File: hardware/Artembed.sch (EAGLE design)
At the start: 88 parts, among them J3 CORTEX_JTAG_DEBUG_MINIMUM_PTH, J4 CORTEX_JTAG_DEBUG_PTH_NS, J7 CAMERA-HIMAX, U1 DAPLINK_KL26Z, U2 16MHz, U3 ARTEMIS_MODULESMD, U4 1.8V, U5 LIS2DH12, Y1 32.768kHz

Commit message: Pre proto review
Waiting on XTAL footprint update from Eli
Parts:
- removed TP2: TEST-POINT3X5, SparkFun-Connectors:TEST-POINT3X5
- added R32, R33, R34: DNP, SparkFun-Resistors:RESISTOR0603
- C10, C9: value 8pF -> 12pF; device SparkFun-Capacitors:CAP-0603 -> SparkFun-Capacitors:12PF-0603-50V-5%
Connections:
- removed net D1_SLSDA: J5.1
- removed net D2_SLSCL: J5.2
- removed net D3_PWM_UARTTX: J5.3, U3.~AD35(TX1/I2SDAT/PDMCLK)
- removed net D4_MISO: J5.4, U3.(SDA0/MISO0/I2SDAT)~D6
- removed net D5_MOSI_CLKOUT: J5.5, U3.(MOSI0/CLKOUT)~D7
- removed net D6_SCLK: J5.6, U3.(SCL0/SCK0)~D5
- removed net SCL_INTERNAL: ECC1.SCL, J7.SCL, U3.(SCL2/SCK2)~D27, U5.SCL/SPC
- removed net SDA_INTERNAL: ECC1.SDA, J7.SDA, U3.(SDA2/MISO2/RX1)~D25, U5.SDA/SDI/SDO
- new net D1: J9.1, U3.~AD29(PDMDATA)
- new net D2: J5.2, U3.~AD13(I2SBCLK/RX1)
- new net D3: J9.2, U3.(SDA2/MISO2/RX1)~D25
- new net D4: J5.3, U3.(SDA0/MISO0/I2SDAT)~D6
- new net D5: J9.3, U3.(SCL2/SCK2)~D27
- new net D6: J5.4, U3.(RX1/SLINT)~D4
- net CAMERA_D0: now also U3.(SDA3/MISO3/RX1)~D43; no longer U3.(MOSI3/RX1)D38
- net CAMERA_D1: now also U3.AD34(CMPRF2/PDMDATA); no longer U3.(SCL4/SCK4/TX1)~D39
- net CAMERA_D2: now also U3.~AD31(SCCCLK); no longer U3.(SDA4/MISO4/RX1)D40
- net CAMERA_D3: now also U3.~AD33(SWO/32KHZ); no longer U3.(BLEIF_IRQ/SWO/I2SWCLK)D41
- net CAMERA_D4: now also U3.(BLEIF_IRQ/SWO/I2SWCLK)D41; no longer U3.(SCL3/SCK3/TX1)~D42
- net CAMERA_D5: now also U3.(MOSI4)~D44; no longer U3.(SDA3/MISO3/RX1)~D43
- net CAMERA_D6: now also U3.(TX1/PDMCLK/SCCIO)~D37; no longer U3.(MOSI4)~D44
- net CAMERA_DVDD_EN: no longer U3.(MOSI1/TX1/PDMCLK)D10
- net CAMERA_HSYNC: now also U3.(SCL3/SCK3/TX1)~D42; no longer U3.(RX1/TRIG1/PDMDATA)D36
- net CAMERA_INT: now also U3.(MOSI3/RX1)D38; no longer U3.(TX1/32KHZ/SWO)~D24
- net CAMERA_MCLK: now also U3.(CMPIN1/SCCIO)~D18; no longer U3.(SCCRST)~D26
- net CAMERA_PCLK: now also U3.(RX1/TRIG1/PDMDATA)D36; no longer U3.(MOSI2/I2SWCLK)~D28
- net CAMERA_TRIG: now also U3.(CMPRF1/TRIG1/SCCCLK)D17; no longer U3.(I2SWCLK/CMPOUT)~D23
- net CAMERA_VSYNC: now also U3.AD16(TRIG0/SCCRST); no longer U3.(TX1/PDMCLK/SCCIO)~D37
- net D10: now also J5.6, U3.(SLMISO)D2; no longer J9.4, U3.(SLNCE/I2SWCLK)D3
- net D11: now also J9.6, U3.(SLMOSI/SLSDA)D1; no longer J9.5, U3.(SLMISO)D2
- net D12: now also J5.7, U3.(SLSCK/SLSCL/CLKOUT)D0; no longer J9.6, U3.(SLMOSI/SLSDA)D1
- net D13: now also U3.(SLNCE/I2SWCLK)D3; no longer U3.(SLSCK/SLSCL/CLKOUT)D0
- net D7: now also J9.4, U3.~AD35(TX1/I2SDAT/PDMCLK); no longer J9.1, U3.~AD13(I2SBCLK/RX1)
- net D8: now also J5.5, U3.(MOSI0/CLKOUT)~D7; no longer J9.2, U3.~AD29(PDMDATA)
- net D9: now also J9.5, U3.(SCL0/SCK0)~D5; no longer J9.3, U3.(RX1/SLINT)~D4
- net N$20: no longer TP2.1
- net SCL: now also ECC1.SCL, J7.SCL, U5.SCL/SPC
- net SDA: now also ECC1.SDA, J7.SDA, U5.SDA/SDI/SDO
- net TGT_SWCLK: now also R33.1
- net TGT_SWDIO: now also R32.1
- net TGT_SWO: now also R34.1
- net VDD: now also J5.1, R32.2, R33.2, R34.2; no longer J5.7
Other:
- moved on the sheet: J3, J5, J9

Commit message: proto review revisions, panelized, cammed
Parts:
- added FD1, FD2, FD3, FD4: FIDUCIAL0.2MM, SparkFun-Aesthetics:FIDUCIAL0.2MM
- added LOGO1: OSHW-LOGOS, SparkFun-Aesthetics:OSHW-LOGOS
- added LOGO2: SFE_LOGO_NAME.2_INCH, SparkFun-Aesthetics:SFE_LOGO_NAME.2_INCH
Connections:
- net CAMERA_DVDD_EN: now also U3.(ADCD1N/RX1/PDMDATA)D15

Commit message: initial commit of v02 schematic
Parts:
- removed C21: 1.0uF, SparkFun-Capacitors:1.0UF-0603-16V-10%
- removed D7: RED, SparkFun-LED:LED-RED0603
- removed E2: SPH0641LM4H-1, SparkFun-Sensors:SPH0641LM4H-1_MICROPHONE
- removed ECC1: ATECC508AUDFN_2X3MM, ATECC508A:ATECC508AUDFN_2X3MM
- removed FD1, FD2, FD3, FD4: FIDUCIAL0.2MM, SparkFun-Aesthetics:FIDUCIAL0.2MM
- removed JP1: HW/SW RESET, SparkFun-Jumpers:JUMPER-SMT_3_1-NC_TRACE_SILK
- removed LOGO1: OSHW-LOGOS, SparkFun-Aesthetics:OSHW-LOGOS
- removed LOGO2: SFE_LOGO_NAME.2_INCH, SparkFun-Aesthetics:SFE_LOGO_NAME.2_INCH
- removed R21: 2.2k, SparkFun-Resistors:2.2KOHM-0603-1/10W-1%
- removed R22, R30: 10k, SparkFun-Resistors:10KOHM-0603-1/10W-1%
- removed R23, R29: 33, SparkFun-Resistors:33OHM-0603-1/10W-1%
- removed R24: 10, SparkFun-Resistors:10OHM-0603-1/10W-1%
- removed R25, R26, R27, R28: 330, SparkFun-Resistors:330OHM-0603-1/10W-1%
- removed R32, R33, R34: DNP, SparkFun-Resistors:RESISTOR0603
- removed S3: RESET IF, SparkFun-Switches:MOMENTARY-SWITCH-SPST-SMD-4.6X2.8MM
- removed TP12, TP13: TEST-POINT3X5, SparkFun-Connectors:TEST-POINT3X5
- removed U5: LIS2DH12, SparkFun-Sensors:LIS2DH12
- added E1: SPH0641LM4H-1, SparkFun-Sensors:SPH0641LM4H-1_MICROPHONE
- added J10: (no value), SparkFun-Connectors:CONN_08SMD-STRAIGHT-FEMALE
- added S1: DIP-04SMD, SparkFun-Switches:DIP-04SMD
- added X1: 16MHz, SparkFun-Clocks:CRYSTAL-16MHZ_SMALL
- C1, C17: value 0.1uF -> 10uF; device SparkFun-Capacitors:0.1UF-0603-25V-5% -> SparkFun-Capacitors:10UF-0603-6.3V-20%
- C10: value 12pF -> 15pF; device SparkFun-Capacitors:12PF-0603-50V-5% -> SparkFun-Capacitors:15PF-0603-50V-5%
- C11: value 0.1uF -> 15pF; device SparkFun-Capacitors:0.1UF-0603-25V-5% -> SparkFun-Capacitors:15PF-0603-50V-5%
- C14: value 15pF -> 0.1uF; device SparkFun-Capacitors:15PF-0603-50V-5% -> SparkFun-Capacitors:0.1UF-0603-25V-5%
- C15: value 15pF -> 1.0uF; device SparkFun-Capacitors:15PF-0603-50V-5% -> SparkFun-Capacitors:1.0UF-0603-16V-10%
- C16, C3: value 1.0uF -> 0.1uF; device SparkFun-Capacitors:1.0UF-0603-16V-10% -> SparkFun-Capacitors:0.1UF-0603-25V-5%
- C18, C2: value 10uF -> 1.0uF; device SparkFun-Capacitors:10UF-0603-6.3V-20% -> SparkFun-Capacitors:1.0UF-0603-16V-10%
- C5: value 1nF -> 2.2uF; device SparkFun-Capacitors:1.0NF/1000PF-0603-50V-10% -> SparkFun-Capacitors:2.2UF-0603-10V-20%
- C6: value 2.2uF -> 0.1uF; device SparkFun-Capacitors:2.2UF-0603-10V-20% -> SparkFun-Capacitors:0.1UF-0603-25V-5%
- C8: value 0.1uF -> 12pF; device SparkFun-Capacitors:0.1UF-0603-25V-5% -> SparkFun-Capacitors:12PF-0603-50V-5%
- D1: value 3A/10V/280mV -> BLUE; device SparkFun-DiscreteSemi:DIODE-SCHOTTKY-BAT60A -> SparkFun-LED:LED-BLUE0603
- D2: value 3A/10V/280mV -> GREEN; device SparkFun-DiscreteSemi:DIODE-SCHOTTKY-BAT60A -> SparkFun-LED:LED-GREEN0603
- D3: value PRTR5V0U2F -> Yellow; device SparkFun-IC-Power:PRTR5V0U2F -> SparkFun-LED:LED-YELLOW0603
- D4: value BLUE -> RED; device SparkFun-LED:LED-BLUE0603 -> SparkFun-LED:LED-RED0603
- D5: value GREEN -> BLUE; device SparkFun-LED:LED-GREEN0603 -> SparkFun-LED:LED-BLUE0603
- D6: value Yellow -> PRTR5V0U2F; device SparkFun-LED:LED-YELLOW0603 -> SparkFun-IC-Power:PRTR5V0U2F
- FRAME1: DESIGNER Owen Lyke -> (none); REV v01 -> (none)
- J1: device SparkFun-Connectors:CONN_02-JST-2MM-SMT -> SparkFun-Connectors:USB_C2-LAYER
- J2: value (none) -> CORTEX_JTAG_DEBUG_MINIMUM_PTH; device SparkFun-Connectors:USB_C2-LAYER -> SparkFun-Connectors:CORTEX_JTAG_DEBUG_MINIMUM_PTH
- J3: value CORTEX_JTAG_DEBUG_MINIMUM_PTH -> CORTEX_JTAG_DEBUG_PTH_NS; device SparkFun-Connectors:CORTEX_JTAG_DEBUG_MINIMUM_PTH -> SparkFun-Connectors:CORTEX_JTAG_DEBUG_PTH_NS
- J4: value CORTEX_JTAG_DEBUG_PTH_NS -> (none); device SparkFun-Connectors:CORTEX_JTAG_DEBUG_PTH_NS -> SparkFun-Connectors:CONN_08SMD-STRAIGHT-FEMALE
- J5: device SparkFun-Connectors:CONN_08NO_SILK_FEMALE_PTH -> SparkFun-Connectors:CONN_08SMD-STRAIGHT-FEMALE
- J6: value (none) -> QWIIC_RIGHT_ANGLE; device SparkFun-Connectors:CONN_07NO_SILK -> SparkFun-Connectors:QWIIC_CONNECTORJS-1MM
- J8: device SparkFun-Connectors:QWIIC_CONNECTORJS-1MM -> SparkFun-Connectors:CONN_08SMD-STRAIGHT-FEMALE
- J9: device SparkFun-Connectors:CONN_07NO_SILK -> SparkFun-Connectors:CONN_08SMD-STRAIGHT-FEMALE
- R1, R2, R3: value 10k -> 330; device SparkFun-Resistors:10KOHM-0603-1/10W-1% -> SparkFun-Resistors:330OHM-0603-1/10W-1%
- R11: value DNP -> 10k; device SparkFun-Resistors:RESISTOR0603 -> SparkFun-Resistors:10KOHM-0603-1/10W-1%
- R12, R13: value 0 -> 10k; device SparkFun-Resistors:0OHM-0603-1/10W -> SparkFun-Resistors:10KOHM-0603-1/10W-1%
- R14: value 5.62k -> 2.2k; device SparkFun-Resistors:5.62KOHM-0603-1/10W-1% -> SparkFun-Resistors:2.2KOHM-0603-1/10W-1%
- R15: value DNP -> 2.2k; device SparkFun-Resistors:RESISTOR0603 -> SparkFun-Resistors:2.2KOHM-0603-1/10W-1%
- R16, R18: value DNP -> 33; device SparkFun-Resistors:RESISTOR0603 -> SparkFun-Resistors:33OHM-0603-1/10W-1%
- R17: value DNP -> 10; device SparkFun-Resistors:RESISTOR0603 -> SparkFun-Resistors:10OHM-0603-1/10W-1%
- R19: value 10k -> 5.62k; device SparkFun-Resistors:10KOHM-0603-1/10W-1% -> SparkFun-Resistors:5.62KOHM-0603-1/10W-1%
- R20: value 2.2k -> 10k; device SparkFun-Resistors:2.2KOHM-0603-1/10W-1% -> SparkFun-Resistors:10KOHM-0603-1/10W-1%
- R4, R5: value 0 -> 330; device SparkFun-Resistors:0OHM-0603-1/10W -> SparkFun-Resistors:330OHM-0603-1/10W-1%
- R6: value 0 -> 5.1k; device SparkFun-Resistors:0OHM-0603-1/10W -> SparkFun-Resistors:5.1KOHM5.1KOHM-0603-1/10W-1%
- R8: value 5.1k -> DNP; device SparkFun-Resistors:5.1KOHM5.1KOHM-0603-1/10W-1% -> SparkFun-Resistors:RESISTOR0603
- R9: value 0 -> DNP; device SparkFun-Resistors:0OHM-0603-1/10W -> SparkFun-Resistors:RESISTOR0603
- S2: value RESET TGT -> TGT_RST
- U2: value 16MHz -> ARTEMIS_MODULESMD; device SparkFun-Clocks:CRYSTAL-16MHZ_SMALL -> SparkFun-IC-Microcontroller:ARTEMIS_MODULESMD
- U3: value ARTEMIS_MODULESMD -> LIS2DH12; device SparkFun-IC-Microcontroller:ARTEMIS_MODULESMD -> SparkFun-Sensors:LIS2DH12
- U4: value 1.8V -> AP2127K-1.8V
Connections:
- removed net !TGT_RST!_HW: C5.1, J3.!RESET, JP1.3, R3.1, S2.2, U3.!RST
- removed net !TGT_RST!_SW: JP1.1, U3.(CMPRF0/SCCCLK/I2SBCLK)~D19
- removed net CAMERA_DVDD_EN: R30.2, U3.(ADCD1N/RX1/PDMDATA)D15, U4.EN
- removed net D1: J9.1, U3.~AD29(PDMDATA)
- removed net D10: J5.6, U3.(SLMISO)D2
- removed net D11: J9.6, U3.(SLMOSI/SLSDA)D1
- removed net D12: J5.7, U3.(SLSCK/SLSCL/CLKOUT)D0
- removed net D2: J5.2, U3.~AD13(I2SBCLK/RX1)
- removed net D3: J9.2, U3.(SDA2/MISO2/RX1)~D25
- removed net D4: J5.3, U3.(SDA0/MISO0/I2SDAT)~D6
- removed net D5: J9.3, U3.(SCL2/SCK2)~D27
- removed net D6: J5.4, U3.(RX1/SLINT)~D4
- removed net D7: J9.4, U3.~AD35(TX1/I2SDAT/PDMCLK)
- removed net D8: J5.5, U3.(MOSI0/CLKOUT)~D7
- removed net D9: J9.5, U3.(SCL0/SCK0)~D5
- removed net N$17: R12.1, TP3.1, U1.TGT_TX
- removed net N$18: R13.1, TP4.1, U1.TGT_RX
- removed net N$19: R10.1, U1.WAKE_NREQ
- removed net N$20: R22.2, U3.~BOOT(MOSI5/RX1/32KHZ)
- removed net N$21: D2.A, J1.2, TP12.1
- removed net N$22: R9.1, U1.TGT_NRESET
- new net !TGT_RST!_IF: S1.4B, U1.NRESET_FB_ISP
- new net D16: J5.7, U2.AD16(TRIG0/SCCRST)
- new net D23_LED: J9.8, R5.2, U2.(I2SWCLK/CMPOUT)~D23
- new net D24: J9.7, U2.(TX1/32KHZ/SWO)~D24
- new net D25: J9.6, U2.(SDA2/MISO2/RX1)~D25
- new net D26: J9.5, U2.(SCCRST)~D26
- new net D27: J9.4, U2.(SCL2/SCK2)~D27
- new net D28: J9.3, U2.(MOSI2/I2SWCLK)~D28
- new net D29: J5.6, U2.~AD29(PDMDATA)
- new net D31: J5.5, U2.~AD31(SCCCLK)
- new net D32: J5.4, U2.~AD32(SCCIO)
- new net D33: J5.3, U2.~AD33(SWO/32KHZ)
- new net D34: J5.2, U2.AD34(CMPRF2/PDMDATA)
- new net D35: J5.1, U2.~AD35(TX1/I2SDAT/PDMCLK)
- new net D36: J9.2, U2.(RX1/TRIG1/PDMDATA)D36
- new net D37: J9.1, U2.(TX1/PDMCLK/SCCIO)~D37
- new net D38: J10.8, U2.(MOSI3/RX1)D38
- new net D39: J10.7, U2.(SCL4/SCK4/TX1)~D39
- new net D40: J10.6, U2.(SDA4/MISO4/RX1)D40
- new net D41: J10.5, U2.(BLEIF_IRQ/SWO/I2SWCLK)D41
- new net D42: J10.4, U2.(SCL3/SCK3/TX1)~D42
- new net D43: J10.3, U2.(SDA3/MISO3/RX1)~D43
- new net D44: J10.2, U2.(MOSI4)~D44
- new net D45: J10.1, U2.(SWO/I2SDAT/PDMDATA)~D45
- new net N$6: D5.A, R5.1
- net !RST: now also C14.1, J3.!RESET, R19.1, R20.2; no longer C11.1, J4.!RESET, R14.1, R19.2
- net !TGT_RST: now also C4.1, J2.!RESET, R12.1, S1.4A, S2.2, U2.!RST; no longer C1.1, JP1.2, R1.1, R9.2, S3.2, U1.NRESET_FB_ISP
- net 1.8V: now also C19.1; no longer C16.1
- net 3.3V: now also C1.1, C15.1, C16.1, C17.1, C18.1, C2.1, C3.1, C5.1, E1.VDD, J2.VCC, J3.VCC, J6.2, J7.AVDD, J8.1, J8.2, J8.3, J8.4, R12.2, R3.2, R4.2, R8.2, R9.2, TP10.1, U2.VDD*2, U3.CS, U3.SDO/SA0, U3.VDD, U3.VDD_IO, U4.EN, U4.IN; no longer C8.1, D1.A, J4.VCC, R15.2, R16.2, R17.2, R18.2, R25.2, R26.2, R27.2, R28.2, TP13.1
- net CAMERA_D0: now also U2.(SLSCK/SLSCL/CLKOUT)D0; no longer U3.(SDA3/MISO3/RX1)~D43
- net CAMERA_D1: now also U2.(SLMOSI/SLSDA)D1; no longer U3.AD34(CMPRF2/PDMDATA)
- net CAMERA_D2: now also U2.(SLMISO)D2; no longer U3.~AD31(SCCCLK)
- net CAMERA_D3: now also U2.(SLNCE/I2SWCLK)D3; no longer U3.~AD33(SWO/32KHZ)
- net CAMERA_D4: now also U2.(RX1/SLINT)~D4; no longer U3.(BLEIF_IRQ/SWO/I2SWCLK)D41
- net CAMERA_D5: now also U2.(SCL0/SCK0)~D5; no longer U3.(MOSI4)~D44
- net CAMERA_D6: now also U2.(SDA0/MISO0/I2SDAT)~D6; no longer U3.(TX1/PDMCLK/SCCIO)~D37
- net CAMERA_D7: now also U2.(MOSI0/CLKOUT)~D7; no longer U3.(SWO/I2SDAT/PDMDATA)~D45
- net CAMERA_HSYNC: now also U2.(CMPRF1/TRIG1/SCCCLK)D17; no longer U3.(SCL3/SCK3/TX1)~D42
- net CAMERA_INT: now also U2.(MOSI1/TX1/PDMCLK)D10; no longer U3.(MOSI3/RX1)D38
- net CAMERA_MCLK: now also U2.(CMPIN1/SCCIO)~D18; no longer U3.(CMPIN1/SCCIO)~D18
- net CAMERA_PCLK: now also U2.(CMPRF0/SCCCLK/I2SBCLK)~D19; no longer U3.(RX1/TRIG1/PDMDATA)D36
- net CAMERA_TRIG: now also U2.(ADCD1P/TX1/PDMCLK)D14; no longer U3.(CMPRF1/TRIG1/SCCCLK)D17
- net CAMERA_VSYNC: now also U2.(ADCD1N/RX1/PDMDATA)D15; no longer U3.AD16(TRIG0/SCCRST)
- net D13: now also J5.8, U2.~AD13(I2SBCLK/RX1); no longer J9.7, U3.(SLNCE/I2SWCLK)D3
- net GND: now also C10.1, C11.1, C14.2, C15.2, D4.C, D5.C, D6.2, E1.GND, E1.SEL, J1.GND, J3.GND@3, J3.GND@5, J3.GNDDTCT, J4.1, J4.2, J4.3, J4.4, J4.5, J4.6, J4.7, J4.8, J8.5, J8.6, J8.7, J8.8, R13.1, R20.1, R6.1, U2.GND*6, U3.GND, U3.RES, X1.GND; no longer C10.2, C11.2, C14.1, C15.1, C21.2, D3.2, D7.C, E2.GND, E2.SEL, ECC1.CPAD, ECC1.GND, J1.1, J3.GND, J4.GND@3, J4.GND@5, J4.GNDDTCT, J5.8, J6.2, J6.3, J6.4, J6.5, J6.6, J6.7, J8.1, R19.1, R22.1, R30.1, R8.1, S3.1, U2.GND, U3.GND*6, U5.GND, U5.RES
- net LED_HID: now also D2.C; no longer D5.C
- net LED_MSD: now also D1.C; no longer D4.C
- net LED_UART: now also D3.C; no longer D6.C
- net N$1: now also D1.A, R1.1; no longer D4.A, R25.1
- net N$10: now also R11.1; no longer R2.1
- net N$11: now also R13.2, U2.~BOOT(MOSI5/RX1/32KHZ); no longer R11.1, U1.SLEEP_NREQ
- net N$13: now also C8.1, X1.1; no longer C9.1, U2.1
- net N$14: now also C10.2, U2.XI; no longer C14.2, U3.XI
- net N$15: now also C11.2, U2.XO; no longer C15.2, U3.XO
- net N$16: now also C9.1, X1.2; no longer C10.1, U2.2
- net N$2: now also D2.A, R2.1; no longer D5.A, R26.1
- net N$23: now also S1.1B; no longer R4.1
- net N$24: now also S1.2B; no longer R5.1
- net N$25: now also S1.3B; no longer R6.1
- net N$3: now also D3.A, R3.1; no longer D6.A, R27.1
- net N$4: now also J1.CC2, R6.2; no longer J2.CC2, R7.2
- net N$5: now also J1.CC1, R7.2; no longer J2.CC1, R8.2
- net N$7: now also D4.A, R4.1; no longer D7.A, R28.1
- net N$8: now also D6.4, R16.1; no longer D3.4, R23.1
- net N$9: now also D6.6, R18.1; no longer D3.6, R29.1
- net PDM_CLK: now also E1.CLK, U2.~AD12(PDMCLK/TX1); no longer E2.CLK, U3.~AD12(PDMCLK/TX1)
- net PDM_DATA: now also E1.DATA, U2.~AD11(PDMDATA); no longer E2.DATA, U3.~AD11(PDMDATA)
- net SCL: now also J6.4, R14.1, U2.(SCL1/SCK1/TX1/SCCLK)D8, U3.SCL/SPC; no longer ECC1.SCL, J8.4, R20.1, U3.(SCL1/SCK1/TX1/SCCLK)D8, U5.SCL/SPC
- net SDA: now also J6.3, R15.1, U2.(SDA1/MISO1/RX1/SCCIO)D9, U3.SDA/SDI/SDO; no longer ECC1.SDA, J8.3, R21.1, U3.(SDA1/MISO1/RX1/SCCIO)D9, U5.SDA/SDI/SDO
- net TCLK: now also J3.SWDCLK/TCK; no longer J4.SWDCLK/TCK, R18.1
- net TDI: now also J3.NC/TDI; no longer J4.NC/TDI, R17.1
- net TDO: now also J3.SWO/TDO; no longer J4.SWO/TDO, R16.1
- net TGT_RX: now also TP4.1, U1.TGT_RX, U2.~D49(RX0/SDA5/MISO5); no longer R13.2, U3.~D48(TX0/SCL5/SCK5)
- net TGT_SWCLK: now also J2.SWDCLK, R9.1, S1.1A, U2.D20(SWDCK/TX1); no longer J3.SWDCLK, R33.1, R4.2, U3.D20(SWDCK/TX1)
- net TGT_SWDIO: now also J2.SWDIO, R8.1, S1.2A, U2.D21(SWDIO/RX1/SCCRST); no longer J3.SWDIO, R32.1, R5.2, U3.D21(SWDIO/RX1/SCCRST)
- net TGT_SWO: now also J2.SWO, R10.1, S1.3A, U2.(PDMCLK/SWO)~D22; no longer J3.SWO, R34.1, R6.2, U3.(PDMCLK/SWO)~D22
- net TGT_TX: now also TP3.1, U1.TGT_TX, U2.~D48(TX0/SCL5/SCK5); no longer R12.2, U3.~D49(RX0/SDA5/MISO5)
- net TMS: now also J3.SWDIO/TMS; no longer J4.SWDIO/TMS, R15.1
- net USB_D+_P: now also R16.2; no longer R23.2
- net USB_D+_R: now also D6.3, J1.D+; no longer D3.3, J2.D+
- net USB_D-_P: now also R18.2; no longer R29.2
- net USB_D-_R: now also D6.1, J1.D-; no longer D3.1, J2.D-
- net VBUS_IF: now also D6.5, J1.VBUS, R17.1; no longer D3.5, J2.VBUS, R24.1
- net VBUS_IF2: now also R17.2, R19.2; no longer R14.2, R24.2
- net VDD: now also R14.2, R15.2; no longer C17.1, C18.1, C19.1, C2.1, C21.1, C3.1, C4.1, D1.C, D2.C, E2.VDD, ECC1.VCC, J3.VCC, J5.1, J7.AVDD, J8.2, R20.2, R21.2, R3.2, R32.2, R33.2, R34.2, TP10.1, U3.VDD*2, U4.IN, U5.CS, U5.SDO/SA0, U5.VDD, U5.VDD_IO
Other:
- note removed: "I2C Address: 0x60"
- moved on the sheet: C1, C10, C11, C12, C13, C14, C15, C16, C17, C18, C19, C2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

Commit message: work check 03/02
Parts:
- removed R10, R8, R9: DNP, SparkFun-Resistors:RESISTOR0603
- removed TP1, TP10, TP9: TEST-POINT3X5, SparkFun-Connectors:TEST-POINT3X5
- added J11: (no value), SparkFun-Connectors:CONN_08SMD-COMBO-FEMALE
- added J12: (no value), SparkFun-Connectors:CONN_08NO_SILK_FEMALE_PTH
- added J14, J22, J23, J24, J25, J26: (no value), SparkFun-Connectors:CONN_12NO_SILK
- added JP1: JUMPER-SMT_2_NC_TRACE_SILK, SparkFun-Jumpers:JUMPER-SMT_2_NC_TRACE_SILK
- J10, J4: device SparkFun-Connectors:CONN_08SMD-STRAIGHT-FEMALE -> SparkFun-Connectors:CONN_08SMD-COMBO-FEMALE
- J5, J9: value (none) -> 1X04_SMD_STRAIGHT_COMBO; device SparkFun-Connectors:CONN_08SMD-STRAIGHT-FEMALE -> SparkFun-Connectors:CONN_04SMD_STRAIGHT_COMBO
- J8: device SparkFun-Connectors:CONN_08SMD-STRAIGHT-FEMALE -> SparkFun-Connectors:CONN_08NO_SILK_FEMALE_PTH
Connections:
- removed net N$23: S1.1B, U1.TGT_SWCLK
- removed net N$24: S1.2B, U1.TGT_SWDIO
- removed net N$25: S1.3B, U1.TGT_SWO
- new net N$12: S1.4A, U1.TGT_SWO
- new net N$17: S1.3A, U1.TGT_SWDIO
- new net N$18: S1.2A, U1.TGT_SWCLK
- new net TGT_BOOT: JP1.2, R13.2, U2.~BOOT(MOSI5/RX1/32KHZ)
- net !RST: now also R20.1; no longer R20.2
- net !TGT_RST: now also S1.1B; no longer S1.4A
- net !TGT_RST!_IF: now also S1.1A; no longer S1.4B
- net 1.8V: now also J12.8, J4.8, J8.8; no longer TP1.1
- net 3.3V: now also J12.6, J12.7, J4.6, J4.7, J8.6, J8.7; no longer J8.1, J8.2, J8.3, J8.4, R10.2, R8.2, R9.2, TP10.1
- net D13: now also J22.12, J26.12, J5.4; no longer J5.8
- net D16: now also J22.11, J26.11, J5.3; no longer J5.7
- net D23_LED: now also J10.4, J22.4, J26.4; no longer J9.8
- net D24: now also J10.3, J22.3, J26.3; no longer J9.7
- net D25: now also J10.2, J22.2, J26.2; no longer J9.6
- net D26: now also J10.1, J22.1, J26.1; no longer J9.5
- net D27: now also J11.8, J14.12, J25.12; no longer J9.4
- net D28: now also J11.7, J14.11, J25.11; no longer J9.3
- net D29: now also J22.10, J26.10, J5.2; no longer J5.6
- net D31: now also J22.9, J26.9, J5.1; no longer J5.5
- net D32: now also J10.8, J22.8, J26.8; no longer J5.4
- net D33: now also J10.7, J22.7, J26.7; no longer J5.3
- net D34: now also J10.6, J22.6, J26.6; no longer J5.2
- net D35: now also J10.5, J22.5, J26.5; no longer J5.1
- net D36: now also J11.6, J14.10, J25.10; no longer J9.2
- net D37: now also J11.5, J14.9, J25.9; no longer J9.1
- net D38: now also J11.4, J14.8, J25.8; no longer J10.8
- net D39: now also J11.3, J14.7, J25.7; no longer J10.7
- net D40: now also J11.2, J14.6, J25.6; no longer J10.6
- net D41: now also J11.1, J14.5, J25.5; no longer J10.5
- net D42: now also J14.4, J25.4, J9.4; no longer J10.4
- net D43: now also J14.3, J25.3, J9.3; no longer J10.3
- net D44: now also J14.2, J25.2, J9.2; no longer J10.2
- net D45: now also J14.1, J25.1, J9.1; no longer J10.1
- net GND: now also J23.1, J23.10, J23.11, J23.12, J23.2, J23.3, J23.4, J23.5, J23.6, J23.7, J23.8, J23.9, J24.1, J24.10, J24.11, J24.12, J24.2, J24.3, J24.4, J24.5, J24.6, J24.7, J24.8, J24.9, R20.2; no longer J4.1, J4.2, J4.3, J4.4, J4.5, J4.6, J4.7, J4.8, J8.5, J8.6, J8.7, J8.8, R20.1, TP9.1
- net N$11: now also JP1.1, U1.WAKE_NREQ; no longer R13.2, U2.~BOOT(MOSI5/RX1/32KHZ)
- net N$13: now also TP5.1
- net N$16: no longer TP5.1
- net TGT_SWCLK: now also S1.2B; no longer R9.1, S1.1A
- net TGT_SWDIO: now also S1.3B; no longer R8.1, S1.2A
- net TGT_SWO: now also S1.4B; no longer R10.1, S1.3A
- net VBUS_IF2: now also J12.4, J12.5, J4.4, J4.5, J8.4, J8.5
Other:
- moved on the sheet: C10, C11, C18, C4, J10, J2, J4, J8, R12, R13, R14, R15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

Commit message: checkpoint
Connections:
- removed net VDD: R14.2, R15.2
- net 3.3V: now also R14.2, R15.2
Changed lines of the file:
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@@
 <part name="R15" library="SparkFun-Resistors" deviceset="2.2KOHM" device="-0603-1/10W-1%" value="2.2k"/>
 <part name="R14" library="SparkFun-Resistors" deviceset="2.2KOHM" device="-0603-1/10W-1%" value="2.2k"/>
-<part name="SUPPLY11" library="SparkFun-PowerSymbols" deviceset="VDD" device=""/>
-<part name="SUPPLY12" library="SparkFun-PowerSymbols" deviceset="VDD" device=""/>
 <part name="R13" library="SparkFun-Resistors" deviceset="10KOHM" device="-0603-1/10W-1%" value="10k"/>
 <part name="SUPPLY24" library="SparkFun-PowerSymbols" deviceset="3.3V" device=""/>
@@
 <part name="GND23" library="SparkFun-PowerSymbols" deviceset="GND" device=""/>
 <part name="JP1" library="SparkFun-Jumpers" deviceset="JUMPER-SMT_2_NC_TRACE" device="_SILK" package3d_urn="urn:adsk.eagle:package:39281/1"/>
+<part name="SUPPLY11" library="SparkFun-PowerSymbols" deviceset="3.3V" device=""/>
+<part name="SUPPLY12" library="SparkFun-PowerSymbols" deviceset="3.3V" device=""/>
 </parts>
 <sheets>
@@
 <attribute name="VALUE" x="324.104" y="236.22" size="1.778" layer="96" font="vector" rot="R90" align="top-center"/>
 </instance>
-<instance part="SUPPLY11" gate="VDD" x="322.58" y="243.84" smashed="yes">
-<attribute name="VALUE" x="322.58" y="246.634" size="1.778" layer="96" font="vector" align="bottom-center"/>
-</instance>
-<instance part="SUPPLY12" gate="VDD" x="330.2" y="243.84" smashed="yes">
-<attribute name="VALUE" x="330.2" y="246.634" size="1.778" layer="96" font="vector" align="bottom-center"/>
-</instance>
 <instance part="R13" gate="G$1" x="215.9" y="228.6" smashed="yes" rot="R90">
 <attribute name="NAME" x="214.376" y="228.6" size="1.778" layer="95" font="vector" rot="R90" align="bottom-center"/>
@@
 <instance part="JP1" gate="G$1" x="119.38" y="195.58" smashed="yes">
 <attribute name="NAME" x="116.84" y="198.12" size="1.778" layer="95" font="vector"/>
+</instance>
+<instance part="SUPPLY11" gate="G$1" x="322.58" y="243.84" smashed="yes">
+<attribute name="VALUE" x="322.58" y="246.634" size="1.778" layer="96" font="vector" align="bottom-center"/>
+</instance>
+<instance part="SUPPLY12" gate="G$1" x="330.2" y="243.84" smashed="yes">
+<attribute name="VALUE" x="330.2" y="246.634" size="1.778" layer="96" font="vector" align="bottom-center"/>
 </instance>
 </instances>
@@
 <pinref part="J12" gate="G$1" pin="7"/>
 </segment>
+<segment>
+<pinref part="R14" gate="G$1" pin="2"/>
+<wire x1="322.58" y1="243.84" x2="322.58" y2="241.3" width="0.1524" layer="91"/>
+<pinref part="SUPPLY11" gate="G$1" pin="3.3V"/>
+</segment>
+<segment>
+<pinref part="R15" gate="G$1" pin="2"/>
+<wire x1="330.2" y1="243.84" x2="330.2" y2="241.3" width="0.1524" layer="91"/>
+<pinref part="SUPPLY12" gate="G$1" pin="3.3V"/>
+</segment>
 </net>
 <net name="LED_MSD" class="0">
@@
 </segment>
 </net>
-<net name="VDD" class="0">
-<segment>
-<pinref part="R14" gate="G$1" pin="2"/>
-<wire x1="322.58" y1="243.84" x2="322.58" y2="241.3" width="0.1524" layer="91"/>
-<pinref part="SUPPLY11" gate="VDD" pin="VDD"/>
-</segment>
-<segment>
-<pinref part="R15" gate="G$1" pin="2"/>
-<wire x1="330.2" y1="243.84" x2="330.2" y2="241.3" width="0.1524" layer="91"/>
-<pinref part="SUPPLY12" gate="VDD" pin="VDD"/>
-</segment>
-</net>

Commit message: routed gpio
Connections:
- net D13: now also J11.1, J14.5, J25.5; no longer J22.12, J26.12, J5.4
- net D16: now also J22.12, J26.12, J5.4; no longer J22.11, J26.11, J5.3
- net D23_LED: now also J14.3, J25.3, J9.3; no longer J10.4, J22.4, J26.4
- net D24: now also J14.1, J25.1, J9.1; no longer J10.3, J22.3, J26.3
- net D25: now also J11.7, J14.11, J25.11; no longer J10.2, J22.2, J26.2
- net D26: now also J11.6, J14.10, J25.10; no longer J10.1, J22.1, J26.1
- net D27: now also J14.4, J25.4, J9.4; no longer J11.8, J14.12, J25.12
- net D28: now also J11.8, J14.12, J25.12; no longer J11.7, J14.11, J25.11
- net D29: now also J11.4, J14.8, J25.8; no longer J22.10, J26.10, J5.2
- net D31: now also J22.11, J26.11, J5.3; no longer J22.9, J26.9, J5.1
- net D32: now also J11.3, J14.7, J25.7; no longer J10.8, J22.8, J26.8
- net D33: now also J11.2, J14.6, J25.6; no longer J10.7, J22.7, J26.7
- net D34: now also J11.5, J14.9, J25.9; no longer J10.6, J22.6, J26.6
- net D35: now also J14.2, J25.2, J9.2; no longer J10.5, J22.5, J26.5
- net D36: now also J10.6, J22.6, J26.6; no longer J11.6, J14.10, J25.10
- net D37: now also J10.4, J22.4, J26.4; no longer J11.5, J14.9, J25.9
- net D38: now also J10.5, J22.5, J26.5; no longer J11.4, J14.8, J25.8
- net D39: now also J10.1, J22.1, J26.1; no longer J11.3, J14.7, J25.7
- net D40: now also J10.2, J22.2, J26.2; no longer J11.2, J14.6, J25.6
- net D41: now also J22.10, J26.10, J5.2; no longer J11.1, J14.5, J25.5
- net D42: now also J10.7, J22.7, J26.7; no longer J14.4, J25.4, J9.4
- net D43: now also J10.8, J22.8, J26.8; no longer J14.3, J25.3, J9.3
- net D44: now also J10.3, J22.3, J26.3; no longer J14.2, J25.2, J9.2
- net D45: now also J22.9, J26.9, J5.1; no longer J14.1, J25.1, J9.1

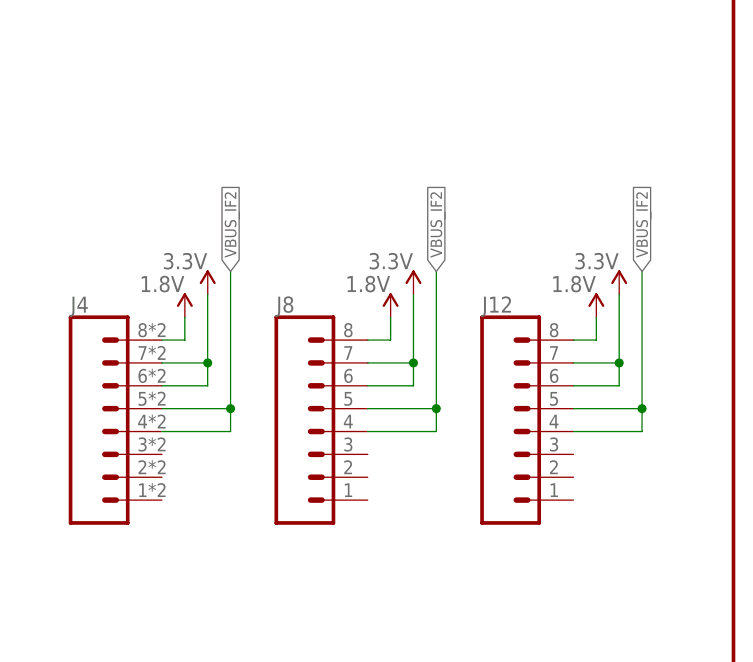
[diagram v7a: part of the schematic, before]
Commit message: ground purs and all airwires gone
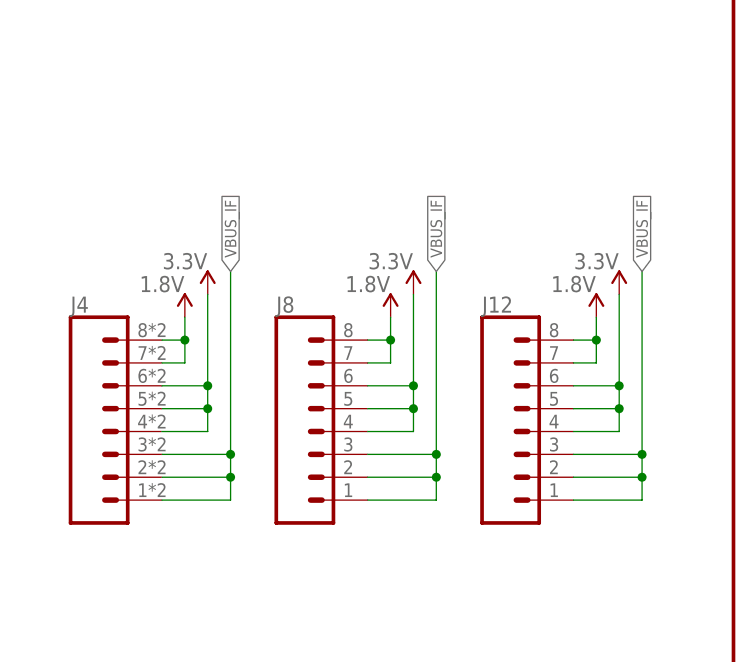
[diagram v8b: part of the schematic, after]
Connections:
- net 1.8V: now also J12.7, J4.7, J8.7
- net 3.3V: now also J12.4, J12.5, J4.4, J4.5, J8.4, J8.5; no longer J12.7, J4.7, J8.7
- net VBUS_IF: now also J12.1, J12.2, J12.3, J4.1, J4.2, J4.3, J8.1, J8.2, J8.3
- net VBUS_IF2: no longer J12.4, J12.5, J4.4, J4.5, J8.4, J8.5
